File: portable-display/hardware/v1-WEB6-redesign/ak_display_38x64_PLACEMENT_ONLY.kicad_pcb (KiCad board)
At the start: 4 copper layers, 38 x 64 mm, 124 parts, among them J1 USB4105-GF-A-060, J2 1S LiPo + NTC, J3 DEBUG POGO, J4 KD024EGOIN152-01, J5 MicroSD, Q1 2N7002, Q2 2N7002, Q3 AO3401A, SW1 UP, SW2 DOWN, SW3 OK, SW4 BACK, SW5 POWER, SW6 FEL, U1 AXP2101, U10 TPS65631DPDR, U2 V851s, U3 W25N01GVZEIG, U4 LIS2DW12TR, U5 RV-3028-C7, U6 SN74LVC1G123DCTR, U8 TPS22918DBVR, U9 USBLC6-2SC6, Y1 24MHz 10ppm

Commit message: fix: correct electrical nets and pinouts for U6, VMID, and V851S power domains
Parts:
- moved R12 7.57 mm to (31.0, 8.00), turned to 0 degrees
- moved C23 7.40 mm to (31.0, 9.30), turned to 0 degrees
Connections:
- C38 pad 1: VSYS -> VMID
- U1 pad 36: VSYS -> VMID
- U2 pad 37: SOC_LDO_1V8 -> 1V8
- U2 pad 62: SOC_LDO_1V8 -> 1V8
- U2 pad 79: SOC_LDO_1V8 -> 1V8
- U6 pad 1: WAKE_PULSE -> WAKE_REQ_N
- U6 pad 2: GND -> RTC_3V3
- U6 pad 3: WAKE_CEXT -> RTC_3V3
- U6 pad 4: WAKE_REXT -> GND
- U6 pad 5: WAKE_REQ_N -> WAKE_PULSE
- U6 pad 6: RTC_3V3 -> WAKE_CEXT
- U6 pad 7: RTC_3V3 -> WAKE_REXT

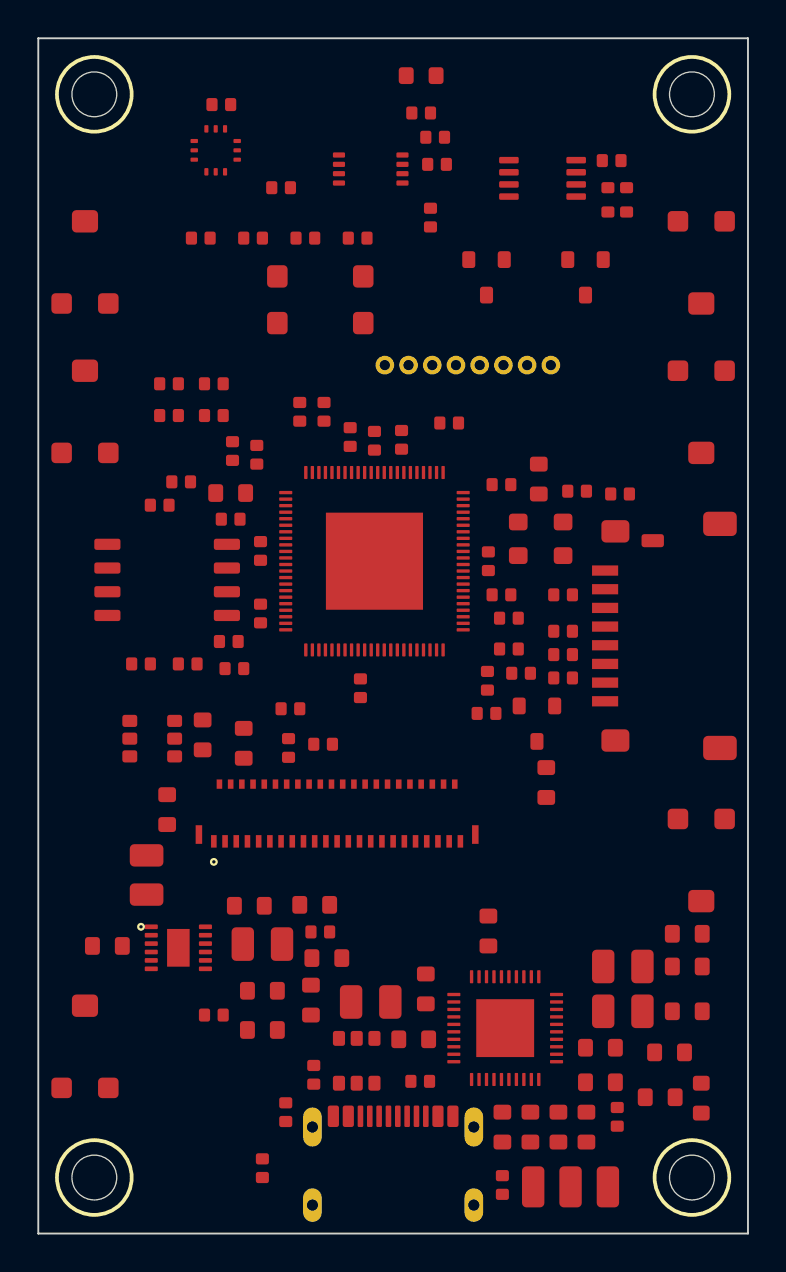
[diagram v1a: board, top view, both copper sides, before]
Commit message: feat: [Grok] implement DRC-aware automatic PCB router
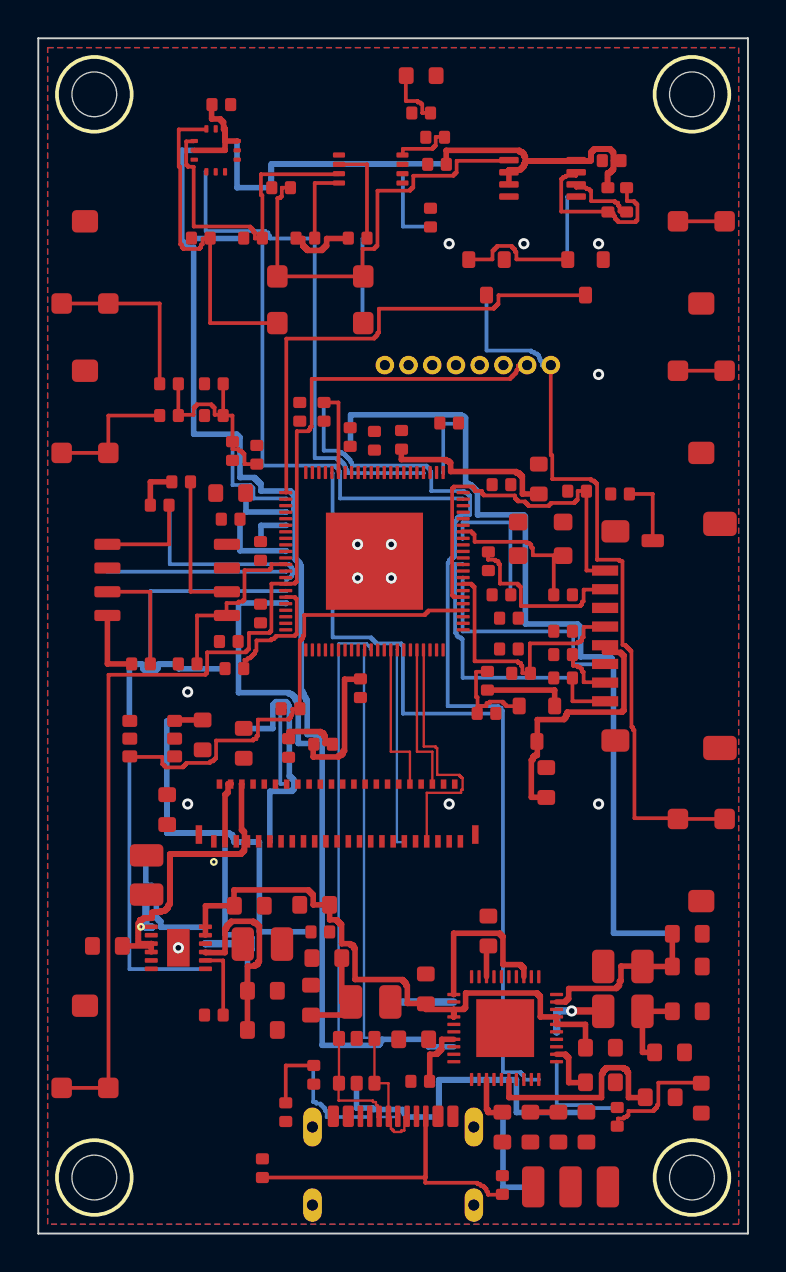
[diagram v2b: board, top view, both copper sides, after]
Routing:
- net RTC_3V3: track 0.00 -> 101.2 mm
- net NAND_MOSI: track 0.00 -> 80.4 mm
- net DRAM_1V5: track 0.00 -> 56.6 mm
- net PMIC_SCL: track 0.00 -> 54.7 mm
- net VSYS: track 0.00 -> 42.5 mm
- net LCD_EN: track 0.00 -> 42.4 mm
- net 3V3: track 0.00 -> 42.3 mm
- net I2C0_SCL: track 0.00 -> 42.2 mm
- net PWRON_N: track 0.00 -> 40.8 mm
- net I2C0_SDA: track 0.00 -> 32.2 mm
- net USB_DM: track 0.00 -> 30.9 mm
- net USB_DP: track 0.00 -> 29.1 mm
- net WAKE_PULSE_N: track 0.00 -> 26.6 mm
- net ELVSS: track 0.00 -> 24.4 mm
- net WAKE_REQ_N: track 0.00 -> 24.2 mm
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- added copper zone on B.Cu, net GND
- added copper zone on F.Cu, net GND
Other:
- board text added: "ROUTED CANDIDATE - NOT FOR FABRICATION"
- board text removed: "PLACEMENT ONLY - NOT FOR FABRICATION"

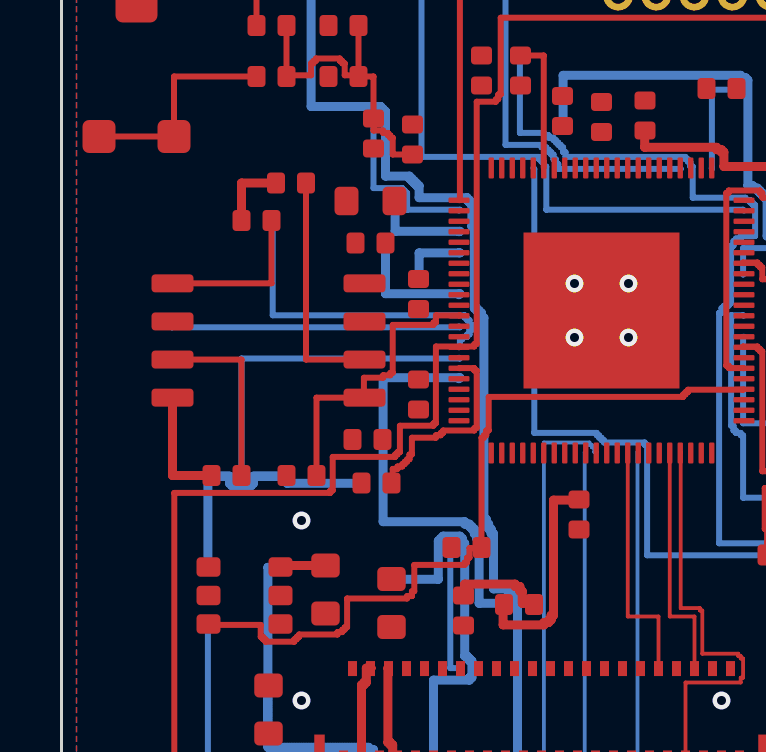
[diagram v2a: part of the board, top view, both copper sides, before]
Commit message: refactor: transition to TF-only boot architecture , removing SPI NAND components
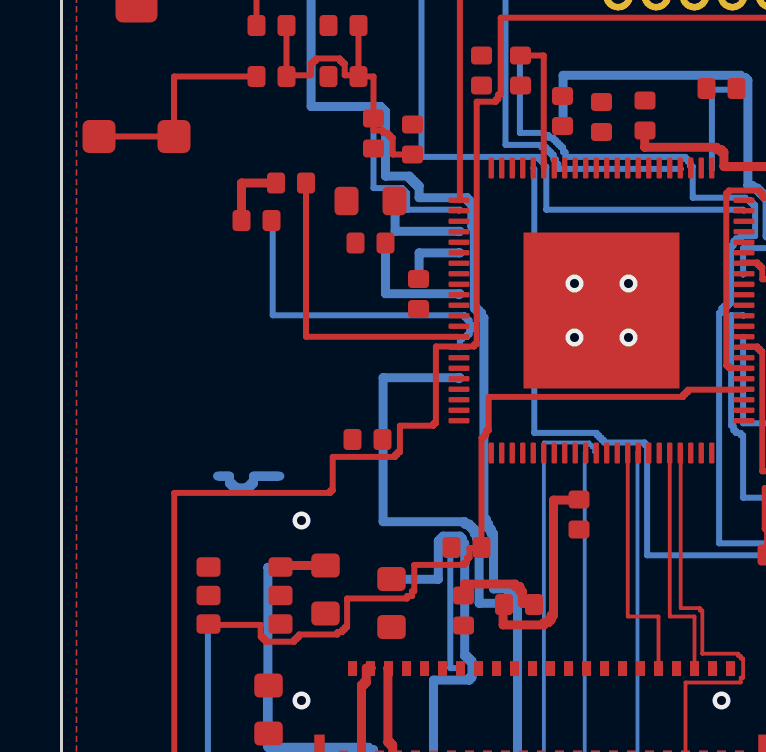
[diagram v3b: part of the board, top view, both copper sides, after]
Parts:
- removed C22: 100n, Sameat:0402
- removed R7, R8, R9: 10k, Sameat:0402
- removed U3: W25N01GVZEIG, Sameat:WSON-8
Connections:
- net NAND_MISO renamed BOOT1
- net NAND_MOSI renamed BOOT0
- U2 pad 56: NAND_CS -> unconnected-(U2-PC1_SPI0_CS-Pad56)
- U2 pad 57: NAND_CLK -> unconnected-(U2-PC0_SPI0_CLK-Pad57)
- U2 pad 60: NAND_HOLD -> unconnected-(U2-PC5_SPI0_HOLD-Pad60)
- U2 pad 61: NAND_WP -> unconnected-(U2-PC4_SPI0_WP-Pad61)
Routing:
- net NAND_HOLD: track 17.4 -> 0.00 mm
- net 3V3: track 42.3 -> 32.1 mm
- net NAND_CS: track 10.2 -> 0.00 mm
- net NAND_CLK: track 9.85 -> 0.00 mm
- net NAND_WP: track 7.27 -> 0.00 mm
- net BOOT0: track 80.4 -> 75.0 mm
- net BOOT1: track 7.84 -> 10.2 mm
